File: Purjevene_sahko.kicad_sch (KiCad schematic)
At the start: 25 parts, among them J1 Conn_Coaxial, J2 XLR2_AudioJack2_Combo, M1 Motor_AC, M2 Autopilot, SW1 Main_switch, SW2 Switchboard

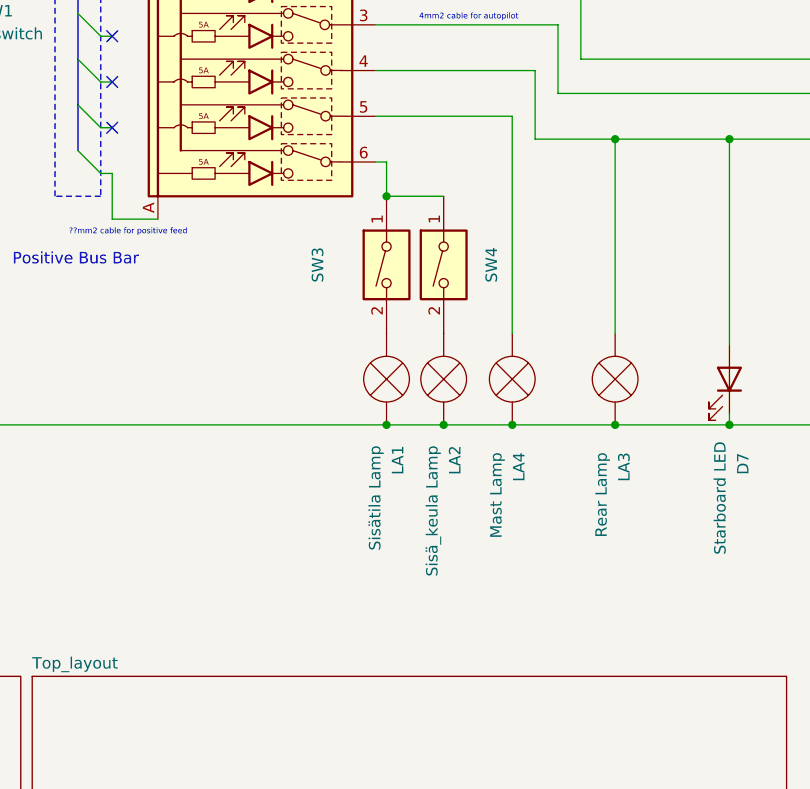
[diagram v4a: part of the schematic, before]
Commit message: Indoor light changed
Indoor light changed to LED
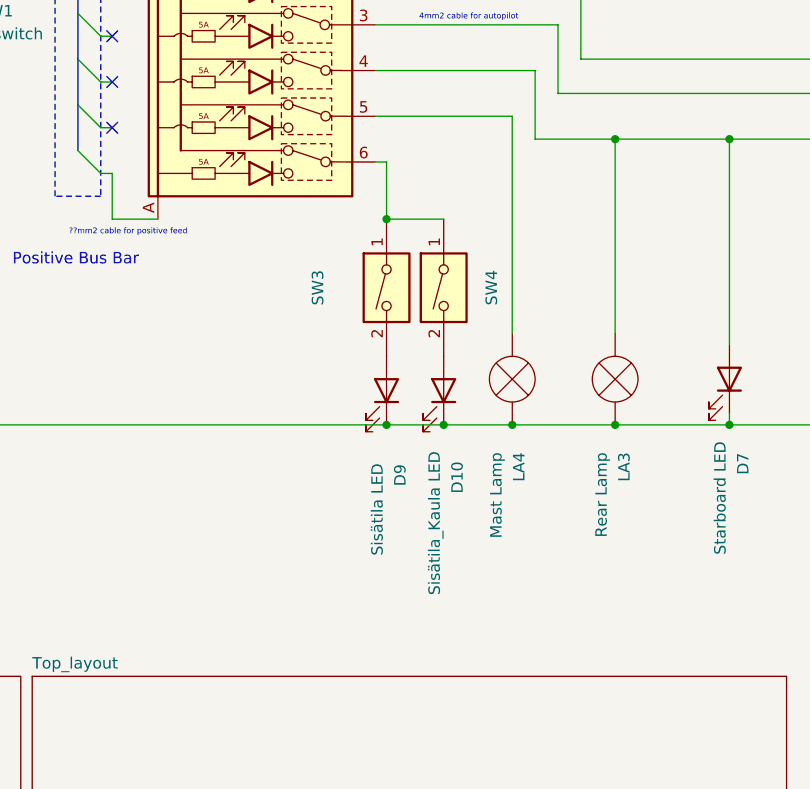
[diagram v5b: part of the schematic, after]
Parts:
- removed LA1: Sisätila Lamp, symbol Device:Lamp
- removed LA2: Sisä_keula Lamp, symbol Device:Lamp
- added D10: Sisätila_Kaula LED, symbol Device:LED
- added D9: Sisätila LED, symbol Device:LED
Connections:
- net at D7.1 (K), D8.1 (K), Instr1.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: now also D10.1 (K), D9.1 (K)
- net at Chrg1. (VDC-): now also PS1.4 (-Vo)
- net at Chrg1.+ (VDC+): now also SC1.1 (+)
- net at SW4.2: now also D10.2 (A)
- net at SW3.2: now also D9.2 (A)
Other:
- moved on the sheet: SW3, SW4

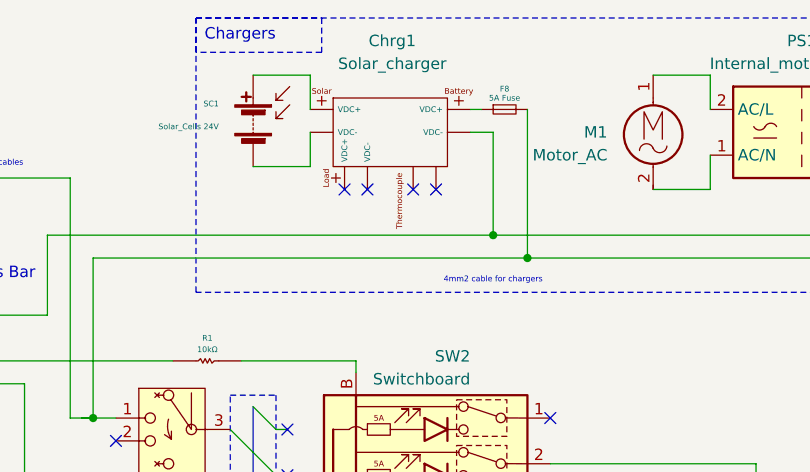
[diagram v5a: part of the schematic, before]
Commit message: Chargers updated
Solar fuse updated to 7.5 and few cables decreased in size
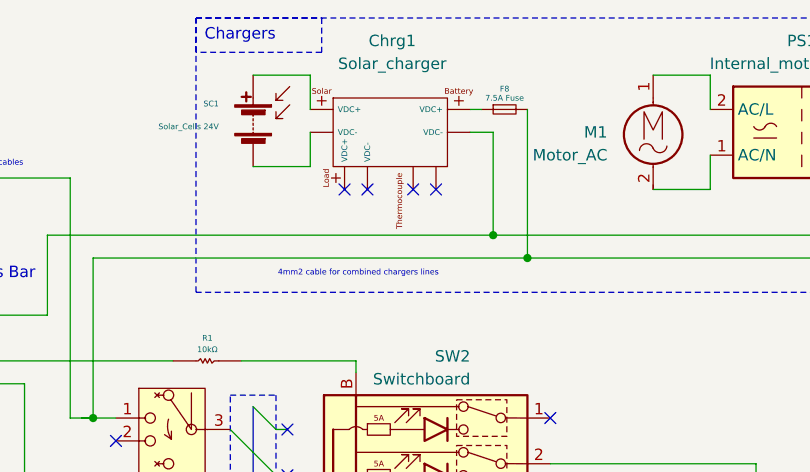
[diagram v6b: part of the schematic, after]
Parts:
- F8: value 5A Fuse -> 7.5A Fuse
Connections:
- net at Chrg1. (VDC-): now also PS1.4 (-Vo)
- net at Chrg1.+ (VDC+): now also SC1.1 (+)
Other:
- note added: "4mm2 cable for combined chargers lines"
- note removed: "4mm2 cable for chargers"

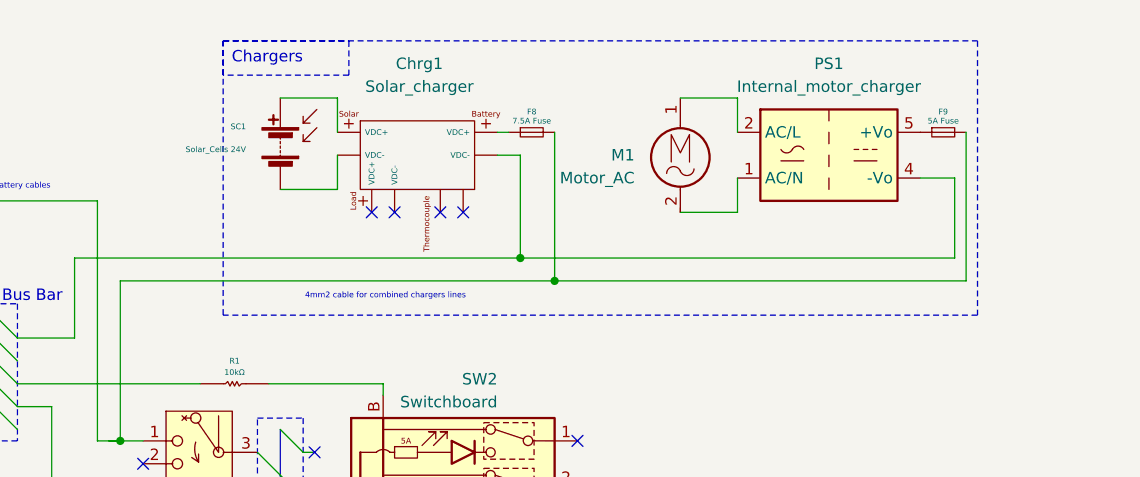
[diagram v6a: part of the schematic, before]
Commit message: Update on charger system
Removed fuses, and added a DC circuit breaker to solar panel PV side
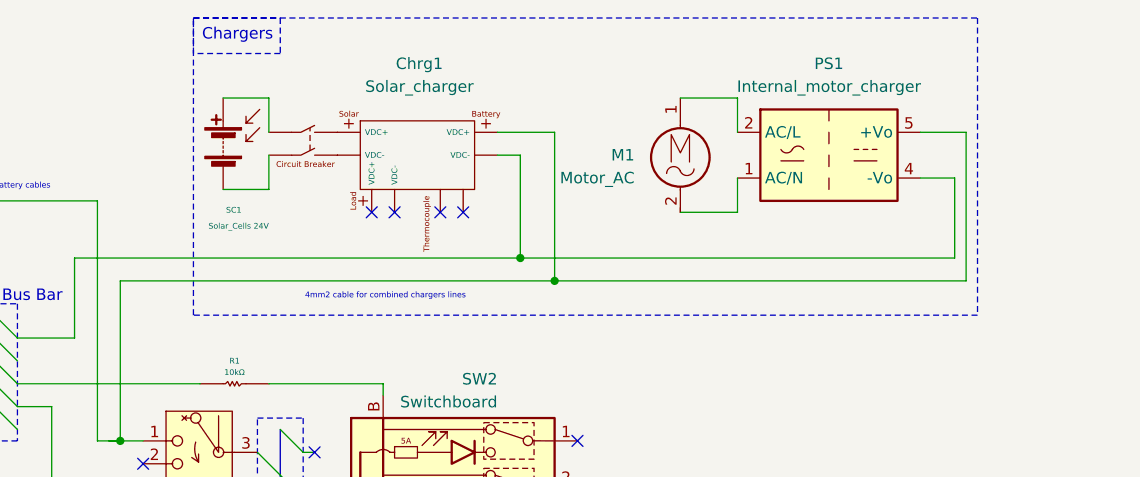
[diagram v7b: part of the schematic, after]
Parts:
- removed F8: 7.5A Fuse, symbol Device:Fuse_Small
- removed F9: 5A Fuse, symbol Device:Fuse_Small
- added CB1: CircuitBreaker_2P, symbol Own:CircuitBreaker_2P
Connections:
- net at PS1.5 (+Vo): now also Chrg1.+ (VDC+), F1.1, SW1.1
- net at Chrg1. (VDC-): now also PS1.4 (-Vo)
- net at SC1.2 (-): now also CB1.; no longer Chrg1. (VDC-)
- net at Chrg1.+ (VDC+): now also CB1.
- net at SC1.1 (+): now also CB1.; no longer Chrg1.+ (VDC+)
- new net: CB1., Chrg1. (VDC-)
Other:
- moved on the sheet: SC1
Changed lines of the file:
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@@
 	)
 	(rectangle
-		(start 91.44 33.02)
+		(start 88.138 30.48)
 		(end 175.26 63.5)
 		(stroke
@@
 	(text_box "Chargers"
 		(exclude_from_sim no)
-		(at 91.44 33.02 0)
-		(size 13.97 3.81)
+		(at 88.138 30.48 0)
+		(size 9.652 3.9483)
 		(margins 0.9525 0.9525 0.9525 0.9525)
 		(stroke
@@
 	(wire
 		(pts
-			(xy 97.79 49.53) (xy 104.14 49.53)
+			(xy 91.44 49.53) (xy 96.52 49.53)
 		)
 		(stroke
@@
 	(wire
 		(pts
+			(xy 91.44 39.37) (xy 96.52 39.37)
+		)
+		(stroke
+			(width 0)
+			(type default)
+			(color 255 0 0 1)
+		)
+	)
+	(wire
+		(pts
 			(xy 151.13 95.25) (xy 151.13 87.63)
 		)
@@
 		)
 	)
-	(bus
+	(wire
 		(pts
-			(xy 97.79 96.52) (xy 97.79 101.6)
+			(xy 96.52 39.37) (xy 96.52 43.18)
 		)
 		(stroke
@@
 		)
 	)
-	(wire
+	(bus
 		(pts
-			(xy 104.14 39.37) (xy 97.79 39.37)
+			(xy 97.79 96.52) (xy 97.79 101.6)
 		)
 		(stroke
-			(width 0.0381)
+			(width 0)
 			(type default)
 			(color 255 0 0 1)
@@
 	(wire
 		(pts
-			(xy 104.14 43.18) (xy 104.14 39.37)
-		)
-		(stroke
-			(width 0.0381)
-			(type default)
-			(color 255 0 0 1)
-		)
-	)
-	(wire
-		(pts
 			(xy 151.13 95.25) (xy 194.31 95.25)
 		)
@@
 	(wire
 		(pts
-			(xy 121.92 43.18) (xy 123.19 43.18)
+			(xy 121.92 43.18) (xy 128.27 43.18)
 		)
 		(stroke
@@
 	(wire
 		(pts
-			(xy 104.14 49.53) (xy 104.14 45.72)
+			(xy 96.52 49.53) (xy 96.52 45.72)
 		)
 		(stroke
@@
 		)
 	)
-	(symbol
-		(lib_id "Device:Fuse_Small")
-		(at 171.45 43.18 0)
-		(unit 1)
-		(body_style 1)
-		(exclude_from_sim no)
-		(in_bom yes)
-		(on_board yes)
-		(in_pos_files yes)
-		(dnp no)
-		(property "Reference" "F9"
-			(at 171.45 40.894 0)
-			(show_name no)
-			(do_not_autoplace no)
-			(effects
-				(font
-					(size 0.635 0.635)
-				)
-			)
-		)
-		(property "Value" "5A Fuse"
-			(at 171.45 41.91 0)
-			(show_name no)
-			(do_not_autoplace no)
-			(effects
-				(font
-					(size 0.635 0.635)
-				)
-			)
-		)
-		(property "Footprint" ""
-			(at 171.45 43.18 0)
-			(hide yes)
-			(show_name no)
-			(do_not_autoplace no)
-			(effects
-				(font
-					(size 1.27 1.27)
-				)
-			)
-		)
-		(property "Datasheet" ""
-			(at 171.45 43.18 0)
-			(hide yes)
-			(show_name no)
-			(do_not_autoplace no)
-			(effects
-				(font
-					(size 1.27 1.27)
-				)
-			)
-		)
-		(property "Description" "Fuse, small symbol"
-			(at 171.45 43.18 0)
-			(hide yes)
-			(show_name no)
-			(do_not_autoplace no)
-			(effects
-				(font
-					(size 1.27 1.27)
-				)
-			)
-		)
-		(pin "2"
-		)
-		(pin "1"
+	(wire
+		(pts
+			(xy 168.91 43.18) (xy 173.99 43.18)
 		)
-		(instances
-			(project "Purjevene_sahko"
-				(path "/fa8154a1-633c-496c-a84e-2f05ab50ac1f"
-					(reference "F9")
-					(unit 1)
-				)
-			)
+		(stroke
+			(width 0.0381)
+			(type default)
+			(color 255 0 0 1)
 		)
 	)
@@
 	)
 	(symbol
-		(lib_id "Device:Fuse_Small")
-		(at 125.73 43.18 0)
-		(unit 1)
-		(body_style 1)
-		(exclude_from_sim no)
-		(in_bom yes)
-		(on_board yes)
-		(in_pos_files yes)
-		(dnp no)
-		(property "Reference" "F8"
-			(at 125.73 40.894 0)
-			(show_name no)
-			(do_not_autoplace no)
-			(effects
-				(font
-					(size 0.635 0.635)
-				)
-			)
-		)
-		(property "Value" "7.5A Fuse"
-			(at 125.73 41.91 0)
-			(show_name no)
-			(do_not_autoplace no)
-			(effects
-				(font
-					(size 0.635 0.635)
-				)
-			)
-		)
-		(property "Footprint" ""
-			(at 125.73 43.18 0)
-			(hide yes)
-			(show_name no)
-			(do_not_autoplace no)
-			(effects
-				(font
-					(size 1.27 1.27)
-				)
-			)
-		)
-		(property "Datasheet" ""
-			(at 125.73 43.18 0)
-			(hide yes)
-			(show_name no)
-			(do_not_autoplace no)
-			(effects
-				(font
-					(size 1.27 1.27)
-				)
-			)
-		)
-		(property "Description" "Fuse, small symbol"
-			(at 125.73 43.18 0)
-			(hide yes)
-			(show_name no)
-			(do_not_autoplace no)
-			(effects
-				(font
-					(size 1.27 1.27)
-				)
-			)
-		)
-		(pin "2"
-		)
-		(pin "1"
-		)
-		(instances
-			(project "Purjevene_sahko"
-				(path "/fa8154a1-633c-496c-a84e-2f05ab50ac1f"
-					(reference "F8")
-					(unit 1)
-				)
-			)
-		)
-	)
-	(symbol
 		(lib_id "Own:Depth_sensor")
 		(at 212.09 109.22 0)
@@
 	(symbol
 		(lib_id "Device:Solar_Cells")
-		(at 97.79 44.45 0)
+		(at 91.44 44.45 0)
 		(mirror y)
 		(unit 1)
@@
 		(in_pos_files yes)
 		(dnp no)
-		(fields_autoplaced yes)
 		(property "Reference" "SC1"
-			(at 93.98 42.5449 0)
+			(at 93.472 51.816 0)
 			(show_name no)
 			(do_not_autoplace no)
@@
 		)
 		(property "Value" "Solar_Cells 24V"
-			(at 93.98 45.0849 0)
+			(at 96.52 53.594 0)
 			(show_name no)
 			(do_not_autoplace no)
@@
 		)
 		(property "Footprint" ""
-			(at 97.79 42.926 90)
+			(at 91.44 42.926 90)
 			(hide yes)
 			(show_name no)
@@
 		)
 		(property "Datasheet" ""
-			(at 97.79 42.926 90)
+			(at 91.44 42.926 90)
 			(hide yes)
 			(show_name no)
@@
 		)
 		(property "Description" "Multiple solar cells"
-			(at 97.79 44.45 0)
+			(at 91.44 44.45 0)
 			(hide yes)
 			(show_name no)
@@
 					(unit 1)
 				)
+			)
+		)
+	)
+	(symbol
+		(lib_id "Own:CircuitBreaker_2P")
+		(at 100.33 44.45 0)
+		(unit 1)
+		(body_style 1)
+		(exclude_from_sim no)
+		(in_bom yes)
+		(on_board yes)
+		(in_pos_files yes)
+		(dnp no)
+		(fields_autoplaced yes)
+		(property "Reference" "CB1"
+			(at 104.14 43.1799 0)
+			(hide yes)
+			(show_name no)
+			(do_not_autoplace no)
+			(effects
+				(font
+					(size 1.27 1.27)
+				)
+				(justify left)
+			)
+		)
+		(property "Value" "CircuitBreaker_2P"
+			(at 104.14 45.7199 0)
+			(hide yes)
+			(show_name no)
+			(do_not_autoplace no)
+			(effects
+				(font
+					(size 1.27 1.27)
+				)
+				(justify left)
+			)
+		)
+		(property "Footprint" ""
+			(at 97.79 44.45 0)
+			(hide yes)
+			(show_name no)
+			(do_not_autoplace no)
+			(effects
+				(font
+					(size 1.27 1.27)
+				)
+			)
+		)
+		(property "Datasheet" ""
+			(at 97.79 44.45 0)
+			(hide yes)
+			(show_name no)
+			(do_not_autoplace no)
+			(effects
+				(font
+					(size 1.27 1.27)
+				)
+			)
+		)
+		(property "Description" "Double pole circuit breaker"
+			(at 100.33 44.45 0)
+			(hide yes)
+			(show_name no)
+			(do_not_autoplace no)
+			(effects
+				(font
+					(size 1.27 1.27)
+				)
+			)
+		)
+		(pin ""
+		)
+		(pin ""
+		)
+		(pin ""
+		)
+		(pin ""
+		)
+		(instances
+			(project "Purjevene_sahko"
+				(path "/fa8154a1-633c-496c-a84e-2f05ab50ac1f"
+					(reference "CB1")
+					(unit 1)
+				)
